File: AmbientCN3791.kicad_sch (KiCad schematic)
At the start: 56 parts, among them J1 Conn_01x02, J2 Conn_01x02, J3 Conn_01x02, J4 Conn_01x04, J5 Conn_01x04, J7 Conn_01x02, J8 Conn_01x02, Q1 AO3401A, Q2 AO3401A, U1 CN3791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

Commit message: Update
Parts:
- added JP10: SolderJumper_2_Open, Jumper:SolderJumper-2_P1.3mm_Open_TrianglePad1.0x1.5mm, symbol Jumper:SolderJumper_2_Open
- C10: footprint Capacitor_SMD:C_0805_2012Metric -> Capacitor_SMD:C_0402_1005Metric; LCSC C1779 -> C23733
- J5, R16, R17: now left out of the parts list
- R18, R19, R20, R21: now not fitted; now left out of the parts list
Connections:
- net CSIN: now also Q1.2 (S), Q2.2 (S); no longer Q1.3 (D), Q2.3 (D)
- net at D3.1 (K), D4.1 (K), L1.1: now also JP10.1 (A)
- new net: D4.2 (A), JP10.2 (B), Q1.3 (D), Q2.3 (D)
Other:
- moved on the sheet: Q1, Q2
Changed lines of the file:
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@@
 	)
 	(junction
+		(at 160.02 48.26)
+		(diameter 0)
+		(color 0 0 0 0)
+	)
+	(junction
 		(at 194.31 45.72)
 		(diameter 0)
@@
 	(wire
 		(pts
+			(xy 160.02 48.26) (xy 160.02 53.34)
+		)
+		(stroke
+			(width 0)
+			(type default)
+		)
+	)
+	(wire
+		(pts
 			(xy 97.79 127) (xy 100.33 127)
 		)
@@
 	(wire
 		(pts
+			(xy 157.48 48.26) (xy 160.02 48.26)
+		)
+		(stroke
+			(width 0)
+			(type default)
+		)
+	)
+	(wire
+		(pts
 			(xy 147.32 121.92) (xy 147.32 127)
 		)
@@
 	(wire
 		(pts
-			(xy 160.02 41.91) (xy 160.02 53.34)
+			(xy 160.02 41.91) (xy 160.02 48.26)
 		)
 		(stroke
@@
 	(wire
 		(pts
+			(xy 147.32 48.26) (xy 149.86 48.26)
+		)
+		(stroke
+			(width 0)
+			(type default)
+		)
+	)
+	(wire
+		(pts
 			(xy 168.91 110.49) (xy 185.42 110.49)
 		)
@@
 	(wire
 		(pts
+			(xy 147.32 41.91) (xy 147.32 48.26)
+		)
+		(stroke
+			(width 0)
+			(type default)
+		)
+	)
+	(wire
+		(pts
 			(xy 187.96 142.24) (xy 187.96 153.67)
 		)
@@
 		(unit 1)
 		(exclude_from_sim no)
-		(in_bom yes)
-		(on_board yes)
-		(dnp no)
+		(in_bom no)
+		(on_board no)
+		(dnp yes)
 		(fields_autoplaced yes)
 		(property "Reference" "R19"
@@
 		(unit 1)
 		(exclude_from_sim no)
-		(in_bom yes)
-		(on_board yes)
-		(dnp no)
+		(in_bom no)
+		(on_board no)
+		(dnp yes)
 		(fields_autoplaced yes)
 		(property "Reference" "R18"
@@
 	(symbol
 		(lib_id "Jumper:SolderJumper_2_Open")
+		(at 153.67 48.26 180)
+		(unit 1)
+		(exclude_from_sim no)
+		(in_bom yes)
+		(on_board yes)
+		(dnp no)
+		(property "Reference" "JP10"
+			(at 153.67 45.212 0)
+			(effects
+				(font
+					(size 1.27 1.27)
+				)
+			)
+		)
+		(property "Value" "SolderJumper_2_Open"
+			(at 153.67 52.07 0)
+			(effects
+				(font
+					(size 1.27 1.27)
+				)
+				(hide yes)
+			)
+		)
+		(property "Footprint" "Jumper:SolderJumper-2_P1.3mm_Open_TrianglePad1.0x1.5mm"
+			(at 153.67 48.26 0)
+			(effects
+				(font
+					(size 1.27 1.27)
+				)
+				(hide yes)
+			)
+		)
+		(property "Datasheet" "~"
+			(at 153.67 48.26 0)
+			(effects
+				(font
+					(size 1.27 1.27)
+				)
+				(hide yes)
+			)
+		)
+		(property "Description" "Solder Jumper, 2-pole, open"
+			(at 153.67 48.26 0)
+			(effects
+				(font
+					(size 1.27 1.27)
+				)
+				(hide yes)
+			)
+		)
+		(pin "1"
+		)
+		(pin "2"
+		)
+		(instances
+			(project "AudioPowerBoard"
+				(path "/8cac44a1-bcd4-4356-b890-bed775abd56a/6c70e4a3-0509-489c-8c5f-252b27900c0f"
+					(reference "JP10")
+					(unit 1)
+				)
+			)
+		)
+	)
+	(symbol
+		(lib_id "Jumper:SolderJumper_2_Open")
 		(at 200.66 49.53 0)
 		(unit 1)
@@
 	(symbol
 		(lib_id "Transistor_FET:AO3401A")
-		(at 139.7 44.45 90)
+		(at 139.7 44.45 270)
+		(mirror x)
 		(unit 1)
 		(exclude_from_sim no)
@@
 		)
 		(property "Footprint" "Package_TO_SOT_SMD:SOT-23"
-			(at 141.605 39.37 0)
+			(at 137.795 39.37 0)
 			(effects
 				(font
@@
 		)
 		(property "Datasheet" "http://www.aosmd.com/pdfs/datasheet/AO3401A.pdf"
-			(at 143.51 39.37 0)
+			(at 135.89 39.37 0)
 			(effects
 				(font
@@
 	(symbol
 		(lib_id "Transistor_FET:AO3401A")
-		(at 139.7 27.94 90)
+		(at 139.7 27.94 270)
+		(mirror x)
 		(unit 1)
 		(exclude_from_sim no)
@@
 		)
 		(property "Footprint" "Package_TO_SOT_SMD:SOT-23"
-			(at 141.605 22.86 0)
+			(at 137.795 22.86 0)
 			(effects
 				(font
@@
 		)
 		(property "Datasheet" "http://www.aosmd.com/pdfs/datasheet/AO3401A.pdf"
-			(at 143.51 22.86 0)
+			(at 135.89 22.86 0)
 			(effects
 				(font
@@
 		(unit 1)
 		(exclude_from_sim no)
-		(in_bom yes)
-		(on_board yes)
+		(in_bom no)
+		(on_board no)
 		(dnp yes)
 		(fields_autoplaced yes)
@@
 		(unit 1)
 		(exclude_from_sim no)
-		(in_bom yes)
-		(on_board yes)
-		(dnp no)
+		(in_bom no)
+		(on_board no)
+		(dnp yes)
 		(fields_autoplaced yes)
 		(property "Reference" "R21"
@@
 		(unit 1)
 		(exclude_from_sim no)
-		(in_bom yes)
-		(on_board yes)
+		(in_bom no)
+		(on_board no)
 		(dnp yes)
 		(fields_autoplaced yes)
@@
 		(unit 1)
 		(exclude_from_sim no)
-		(in_bom yes)
-		(on_board yes)
+		(in_bom no)
+		(on_board no)
 		(dnp yes)
 		(fields_autoplaced yes)
@@
 			)
 		)
-		(property "Footprint" "Capacitor_SMD:C_0805_2012Metric"
+		(property "Footprint" "Capacitor_SMD:C_0402_1005Metric"
 			(at 66.04 129.54 0)
 			(effects
@@
 			)
 		)
-		(property "LCSC" "C1779"
+		(property "LCSC" "C23733"
 			(at 66.04 129.54 0)
 			(effects
@@
 		(unit 1)
 		(exclude_from_sim no)
-		(in_bom yes)
-		(on_board yes)
-		(dnp no)
+		(in_bom no)
+		(on_board no)
+		(dnp yes)
 		(fields_autoplaced yes)
 		(property "Reference" "R20"

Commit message: Update
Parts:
- J3: now not fitted
- R12, R13: now left out of the parts list
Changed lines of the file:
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@@
 		(in_bom yes)
 		(on_board yes)
-		(dnp no)
+		(dnp yes)
 		(fields_autoplaced yes)
 		(property "Reference" "J3"
@@
 		(unit 1)
 		(exclude_from_sim no)
-		(in_bom yes)
-		(on_board yes)
+		(in_bom no)
+		(on_board no)
 		(dnp yes)
 		(fields_autoplaced yes)
@@
 		(unit 1)
 		(exclude_from_sim no)
-		(in_bom yes)
-		(on_board yes)
+		(in_bom no)
+		(on_board no)
 		(dnp yes)
 		(fields_autoplaced yes)

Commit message: Add pdf/
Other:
- company: (none) -> //piernov
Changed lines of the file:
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@@
 	(generator_version "9.0")
 	(paper "A4")
+	(title_block
+		(date "2025-03-04")
+		(rev "v0.1")
+		(company "//piernov")
+	)
 	(text "CTRL"
 		(exclude_from_sim no)

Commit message: Update
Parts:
- J1, J2: footprint Connector_JST:JST_XH_S2B-XH-A_1x02_P2.50mm_Horizontal -> Connector_JST:JST_XH_S2B-XH-A-1_1x02_P2.50mm_Horizontal; FT Rotation Offset (none) -> 180; JLCPCB Rotation Offset 180 -> (none); LCSC C157931 -> C163035
- J3: footprint Connector_JST:JST_XH_S2B-XH-A_1x02_P2.50mm_Horizontal -> Connector_JST:JST_XH_S2B-XH-A-1_1x02_P2.50mm_Horizontal
- JP10: now left out of the parts list
- Q1, Q2: FT Rotation Offset (none) -> 180
- R1: value 200k -> 100k; LCSC C25764 -> C25741
- R2: value 22k -> 10k; LCSC C25768 -> C25744
- RV1: value 50k -> 20k; footprint Potentiometer_THT:Potentiometer_Bourns_3296W_Vertical -> Potentiometer_SMD:Potentiometer_Bourns_3224J_Horizontal; LCSC C118911 -> C27974775
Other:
- note added: "MPPT=1.205V"
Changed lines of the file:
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@@
 		)
 	)
+	(text "MPPT=1.205V"
+		(exclude_from_sim no)
+		(at 85.09 70.104 0)
+		(effects
+			(font
+				(size 1.27 1.27)
+			)
+		)
+	)
 	(text "SOLAR"
 		(exclude_from_sim no)
@@
 			)
 		)
-		(property "Footprint" "Connector_JST:JST_XH_S2B-XH-A_1x02_P2.50mm_Horizontal"
+		(property "Footprint" "Connector_JST:JST_XH_S2B-XH-A-1_1x02_P2.50mm_Horizontal"
 			(at 262.89 41.91 0)
 			(effects
@@
 			)
 		)
-		(property "Value" "22k"
+		(property "Value" "10k"
 			(at 89.154 76.2 0)
 			(effects
@@
 			)
 		)
-		(property "LCSC" "C25768"
+		(property "LCSC" "C25744"
 			(at 93.98 74.93 0)
 			(effects
@@
 			)
 		)
-		(property "Footprint" "Connector_JST:JST_XH_S2B-XH-A_1x02_P2.50mm_Horizontal"
+		(property "Footprint" "Connector_JST:JST_XH_S2B-XH-A-1_1x02_P2.50mm_Horizontal"
 			(at 26.67 41.91 0)
 			(effects
@@
 			)
 		)
-		(property "LCSC" "C157931"
+		(property "LCSC" "C163035"
 			(at 26.67 41.91 0)
 			(effects
@@
 			)
 		)
-		(property "JLCPCB Rotation Offset" "180"
+		(property "FT Rotation Offset" "180"
 			(at 26.67 41.91 0)
 			(effects
@@
 		(unit 1)
 		(exclude_from_sim no)
-		(in_bom yes)
+		(in_bom no)
 		(on_board yes)
 		(dnp no)
@@
 			)
 		)
+		(property "FT Rotation Offset" "180"
+			(at 139.7 44.45 90)
+			(effects
+				(font
+					(size 1.27 1.27)
+				)
+				(hide yes)
+			)
+		)
 		(pin "3"
 		)
@@
 			)
 		)
+		(property "FT Rotation Offset" "180"
+			(at 139.7 27.94 90)
+			(effects
+				(font
+					(size 1.27 1.27)
+				)
+				(hide yes)
+			)
+		)
 		(pin "3"
 		)
@@
 			)
 		)
-		(property "Footprint" "Connector_JST:JST_XH_S2B-XH-A_1x02_P2.50mm_Horizontal"
+		(property "Footprint" "Connector_JST:JST_XH_S2B-XH-A-1_1x02_P2.50mm_Horizontal"
 			(at 233.68 41.91 0)
 			(effects
@@
 			)
 		)
-		(property "LCSC" "C157931"
+		(property "LCSC" "C163035"
 			(at 233.68 41.91 0)
 			(effects
@@
 			)
 		)
-		(property "JLCPCB Rotation Offset" "180"
+		(property "FT Rotation Offset" "180"
 			(at 233.68 41.91 0)
 			(effects
@@
 			)
 		)
-		(property "Value" "50k"
+		(property "Value" "20k"
 			(at 102.87 81.2799 0)
 			(effects
@@
 			)
 		)
-		(property "Footprint" "Potentiometer_THT:Potentiometer_Bourns_3296W_Vertical"
+		(property "Footprint" "Potentiometer_SMD:Potentiometer_Bourns_3224J_Horizontal"
 			(at 100.33 80.01 0)
 			(effects
@@
 			)
 		)
-		(property "LCSC" "C118911"
+		(property "LCSC" "C27974775"
 			(at 100.33 80.01 0)
 			(effects
@@
 			)
 		)
-		(property "Value" "200k"
+		(property "Value" "100k"
 			(at 88.138 65.278 0)
 			(effects
@@
 			)
 		)
-		(property "LCSC" "C25764"
+		(property "LCSC" "C25741"
 			(at 93.98 62.23 0)
 			(effects

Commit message: Schematics page name
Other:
- title: (none) -> AmbientCN3791
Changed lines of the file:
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@@
 	(paper "A4")
 	(title_block
+		(title "AmbientCN3791")
 		(date "2025-03-04")
 		(rev "v0.1")

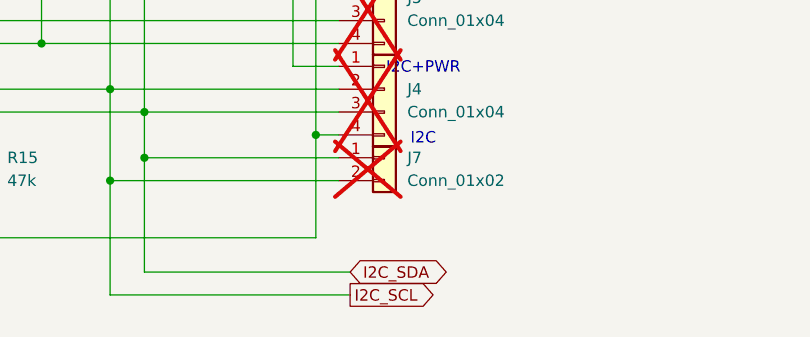
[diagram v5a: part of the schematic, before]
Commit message: v0.2: fix SCL/SDA inversion for INA3221 + fix C8 silkscreen overlap + KiCad 9.0 update
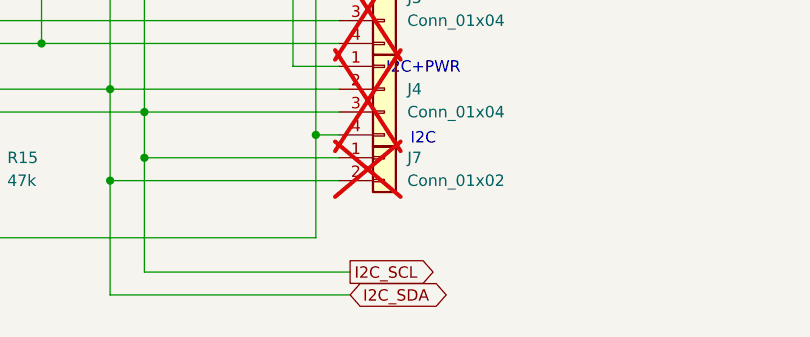
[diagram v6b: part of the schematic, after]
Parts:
- J3: footprint Connector_JST:JST_XH_S2B-XH-A-1_1x02_P2.50mm_Horizontal -> Connector_JST:JST_XH_S2B-XH-A_1x02_P2.50mm_Horizontal
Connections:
- net I2C_SCL: now also J4.3 (Pin_3), J7.1 (Pin_1), R12.1, R17.2, U2.6 (SCL); no longer J4.2 (Pin_2), J7.2 (Pin_2), R13.1, R16.2, U2.7 (SDA)
- net I2C_SDA: now also J4.2 (Pin_2), J7.2 (Pin_2), R13.1, R16.2, U2.7 (SDA); no longer J4.3 (Pin_3), J7.1 (Pin_1), R12.1, R17.2, U2.6 (SCL)
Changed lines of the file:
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@@
 	(title_block
 		(title "AmbientCN3791")
-		(date "2025-03-04")
-		(rev "v0.1")
+		(date "2025-03-31")
+		(rev "v0.2")
 		(company "//piernov")
 	)
@@
 		)
 	)
-	(global_label "I2C_SDA"
-		(shape bidirectional)
-		(at 191.77 157.48 0)
-		(fields_autoplaced yes)
-		(effects
-			(font
-				(size 1.27 1.27)
-			)
-			(justify left)
-		)
-		(property "Intersheetrefs" "${INTERSHEET_REFS}"
-			(at 203.4071 157.48 0)
-			(effects
-				(font
-					(size 1.27 1.27)
-				)
-				(justify left)
-				(hide yes)
-			)
-		)
-	)
 	(global_label "CSOP"
 		(shape input)
@@
 		)
 	)
-	(global_label "CSOP"
-		(shape input)
-		(at 194.31 33.02 90)
+	(global_label "I2C_SDA"
+		(shape bidirectional)
+		(at 191.77 160.02 0)
 		(fields_autoplaced yes)
 		(effects
@@
 		)
 		(property "Intersheetrefs" "${INTERSHEET_REFS}"
-			(at 194.31 24.9548 90)
+			(at 203.4071 160.02 0)
 			(effects
 				(font
@@
 		)
 	)
-	(global_label "I2C_SCL"
-		(shape output)
-		(at 191.77 160.02 0)
+	(global_label "CSOP"
+		(shape input)
+		(at 194.31 33.02 90)
 		(fields_autoplaced yes)
 		(effects
@@
 		)
 		(property "Intersheetrefs" "${INTERSHEET_REFS}"
-			(at 202.2353 160.02 0)
+			(at 194.31 24.9548 90)
 			(effects
 				(font
@@
 		)
 	)
+	(global_label "I2C_SCL"
+		(shape output)
+		(at 191.77 157.48 0)
+		(fields_autoplaced yes)
+		(effects
+			(font
+				(size 1.27 1.27)
+			)
+			(justify left)
+		)
+		(property "Intersheetrefs" "${INTERSHEET_REFS}"
+			(at 202.2353 157.48 0)
+			(effects
+				(font
+					(size 1.27 1.27)
+				)
+				(justify left)
+				(hide yes)
+			)
+		)
+	)
 	(global_label "CSON"
 		(shape input)
@@
 			)
 		)
-		(property "Footprint" "Connector_JST:JST_XH_S2B-XH-A-1_1x02_P2.50mm_Horizontal"
+		(property "Footprint" "Connector_JST:JST_XH_S2B-XH-A_1x02_P2.50mm_Horizontal"
 			(at 262.89 41.91 0)
 			(effects

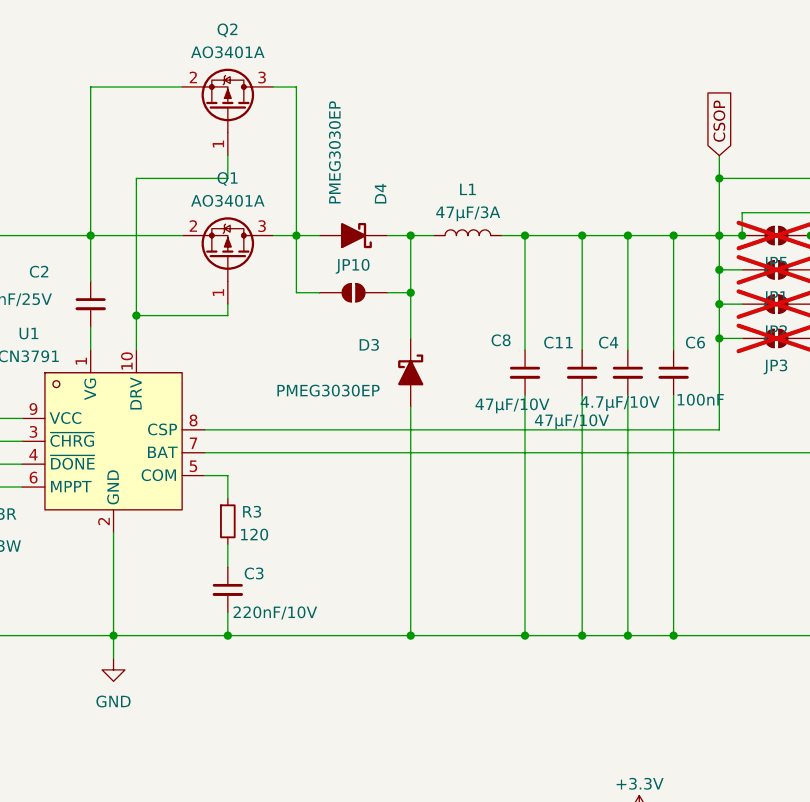
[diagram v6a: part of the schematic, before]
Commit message: v0.2: change diode reference and location for lower leakage + add extra decoupling cap on +3V3 + change potentiometer reference (equivalent) for JLCPCB supply constraint
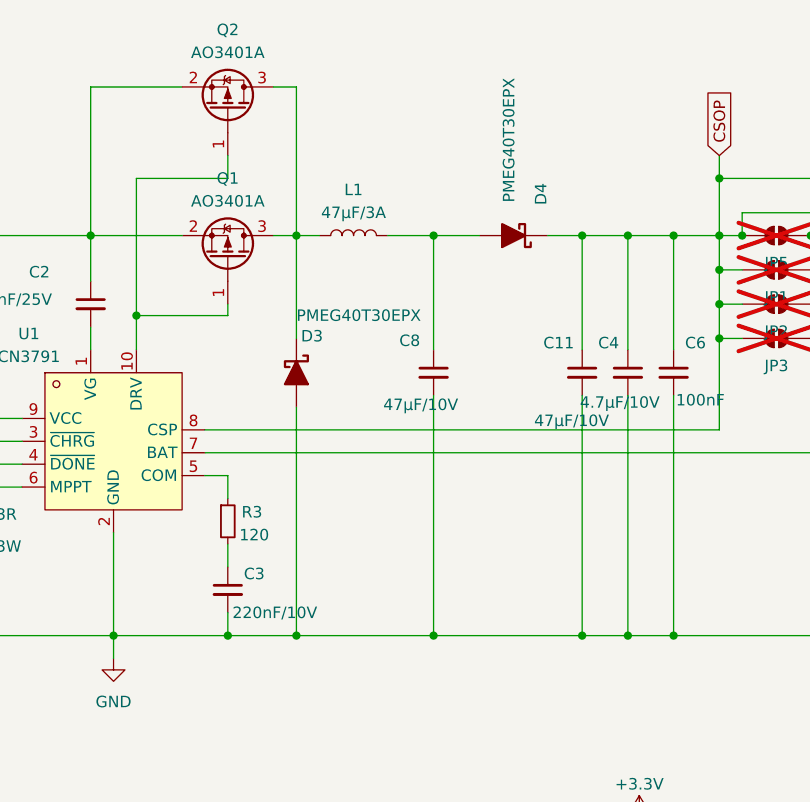
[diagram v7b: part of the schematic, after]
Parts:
- removed JP10: SolderJumper_2_Open, Jumper:SolderJumper-2_P1.3mm_Open_TrianglePad1.0x1.5mm, symbol Jumper:SolderJumper_2_Open
- D3, D4: value PMEG3030EP -> PMEG40T30EPX; LCSC C255587 -> C552919
- RV1: LCSC C27974775 -> C719181
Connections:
- net CSOP: now also D4.1 (K); no longer C8.1, L1.2
- net at D3.1 (K), L1.1: now also Q1.3 (D), Q2.3 (D); no longer D4.1 (K)
- new net: C8.1, D4.2 (A), L1.2
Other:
- moved on the sheet: C8, D3, D4, L1

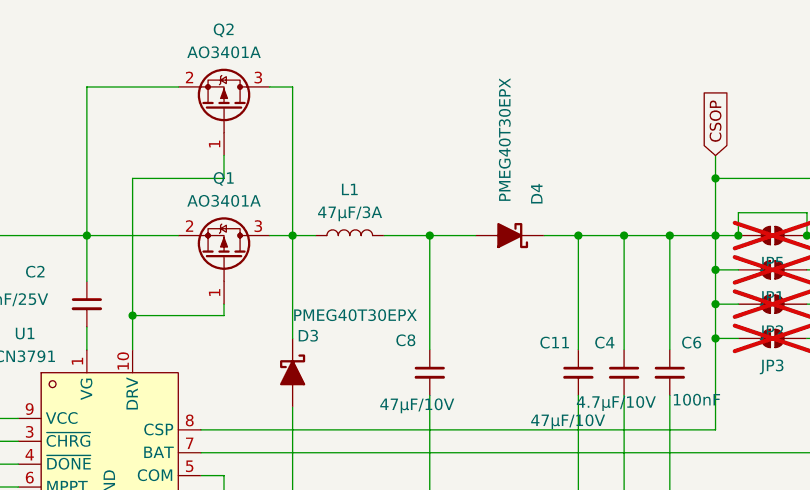
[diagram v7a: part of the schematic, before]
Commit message: v0.3: replace PMEG40T30EPX with PMEG6030EP,115 for supply constraint
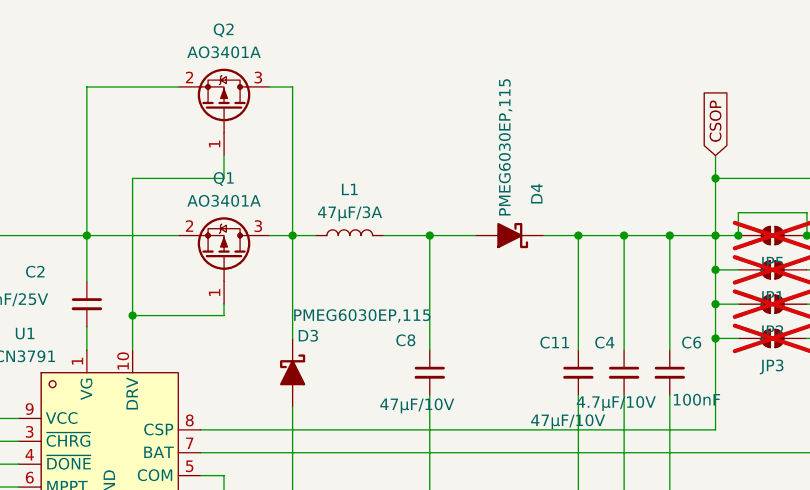
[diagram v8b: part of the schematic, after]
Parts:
- D3, D4: value PMEG40T30EPX -> PMEG6030EP,115; LCSC C552919 -> C456127
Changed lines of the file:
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@@
 	(title_block
 		(title "AmbientCN3791")
-		(date "2025-03-31")
-		(rev "v0.2")
+		(date "2025-07-15")
+		(rev "v0.3")
 		(company "//piernov")
 	)
@@
 			)
 		)
-		(property "Value" "PMEG40T30EPX"
+		(property "Value" "PMEG6030EP,115"
 			(at 170.942 24.384 90)
 			(effects
@@
 			)
 		)
-		(property "LCSC" "C552919"
+		(property "LCSC" "C456127"
 			(at 171.45 41.91 90)
 			(effects
@@
 			)
 		)
-		(property "Value" "PMEG40T30EPX"
+		(property "Value" "PMEG6030EP,115"
 			(at 147.32 50.8 90)
 			(effects
@@
 			)
 		)
-		(property "LCSC" "C552919"
+		(property "LCSC" "C456127"
 			(at 147.32 57.15 90)
 			(effects
